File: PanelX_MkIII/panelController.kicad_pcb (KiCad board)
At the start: 2 copper layers, 35.6 x 22.9 mm, 30 parts, among them J11 Conn_01x05_Male, J12 Conn_01x05_Male, J401 Conn_01x10_Male, J403 Conn_01x10_Male, SW11 SW_SPST, U11 MAX485E, U12 24LC256, U13 ATmega328-A, U14 HEADER_3x2, U26 L78L05_SOT89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

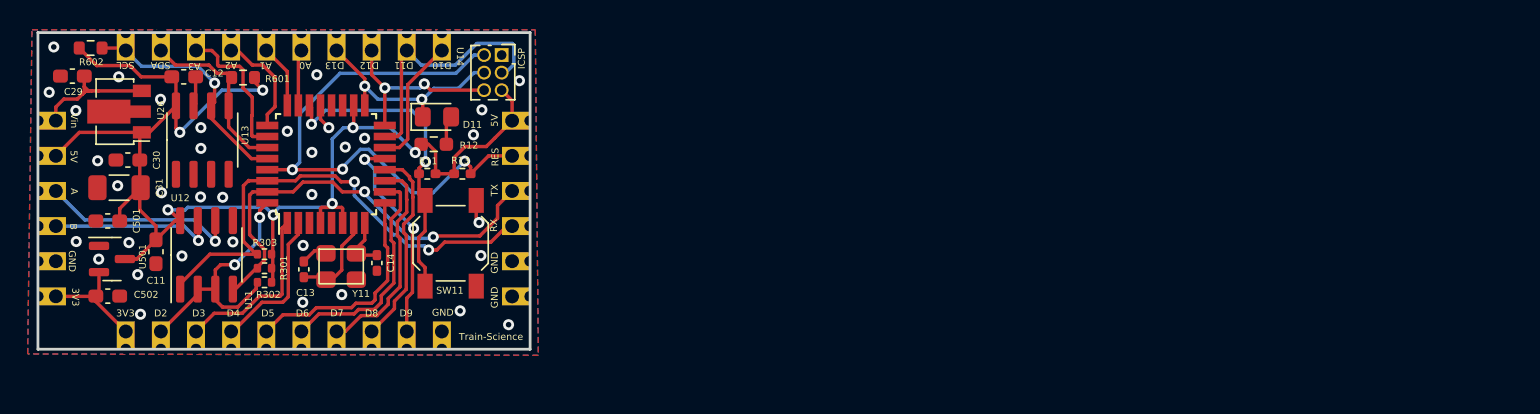
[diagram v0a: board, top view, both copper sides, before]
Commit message: added nano project to repo. Must be modular flatcable design. I want to make 2 versions, one with voltage regulator and Xnet and one as I2C slave
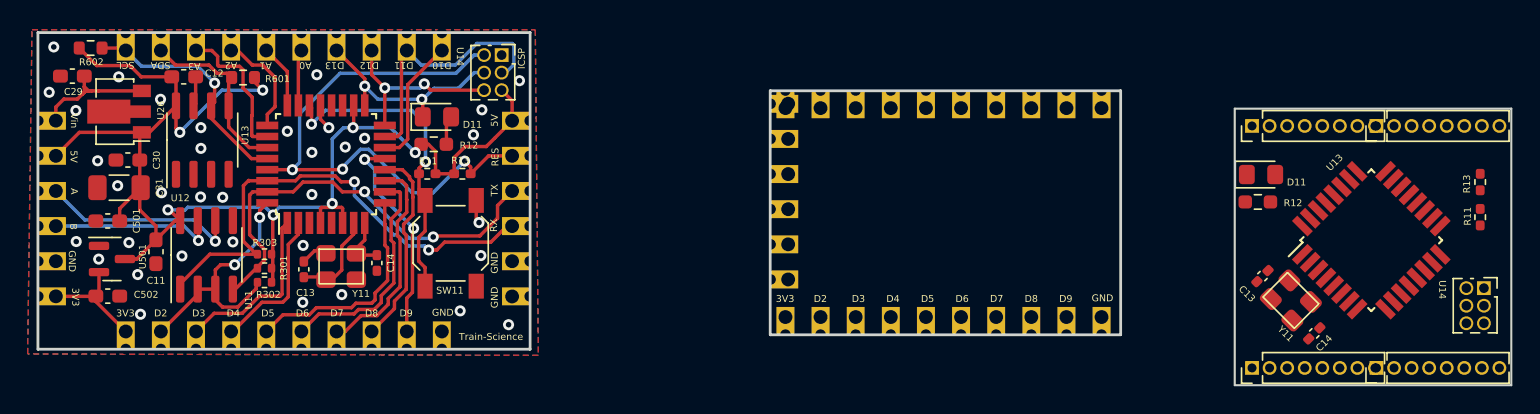
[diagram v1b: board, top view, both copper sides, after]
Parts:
- added C13: 12pF, Capacitor_SMD:C_0402_1005Metric_Pad0.74x0.62mm_HandSolder, F.Cu at (228.3, 106.4)
- added C14: 12pF, Capacitor_SMD:C_0402_1005Metric_Pad0.74x0.62mm_HandSolder, F.Cu at (232.0, 110.5)
- added D11: LED, LED_SMD:LED_0805_2012Metric_Pad1.15x1.40mm_HandSolder, F.Cu at (228.2, 99.0)
- added J11: Conn_01x05_Male, custom_kicad_lib_sk:castellated_2.54mm_01x06, F.Cu at (192.7, 99.0)
- added J401: Conn_01x10_Male, custom_kicad_lib_sk:castellated_2.54mm_01x10, F.Cu at (205.2, 110.6)
- added J403: Conn_01x10_Male, custom_kicad_lib_sk:castellated_2.54mm_01x10, F.Cu at (205.2, 92.9)
- added R11: 10k, Resistor_SMD:R_0402_1005Metric_Pad0.72x0.64mm_HandSolder, F.Cu at (244.0, 102.1)
- added R12: 6k2, Resistor_SMD:R_0603_1608Metric_Pad0.98x0.95mm_HandSolder, F.Cu at (227.9, 101.0)
- added R13: 10k, Resistor_SMD:R_0402_1005Metric_Pad0.72x0.64mm_HandSolder, F.Cu at (244.0, 99.6)
- added REF**: PinHeader_1x08_P1.27mm_Vertical, Connector_PinHeader_1.27mm:PinHeader_1x08_P1.27mm_Vertical, F.Cu at (227.5, 113.0)
- added REF**: PinHeader_1x08_P1.27mm_Vertical, Connector_PinHeader_1.27mm:PinHeader_1x08_P1.27mm_Vertical, F.Cu at (236.5, 95.5)
- added REF**: PinHeader_1x08_P1.27mm_Vertical, Connector_PinHeader_1.27mm:PinHeader_1x08_P1.27mm_Vertical, F.Cu at (236.5, 113.0)
- added REF**: PinHeader_1x08_P1.27mm_Vertical, Connector_PinHeader_1.27mm:PinHeader_1x08_P1.27mm_Vertical, F.Cu at (227.5, 95.5)
- added U13: ATmega328-A, Package_QFP:TQFP-32_7x7mm_P0.8mm, F.Cu at (236.1, 103.8)
- added U14: HEADER_3x2, Connector_PinSocket_1.27mm:PinSocket_2x03_P1.27mm_Vertical, F.Cu at (244.3, 107.2)
- added Y11: crystal_arduino, custom_kicad_lib_sk:crystal_arduino, F.Cu at (230.5, 108.0)
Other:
- board size 35.6 x 22.9 mm -> 106.6 x 25.5 mm
